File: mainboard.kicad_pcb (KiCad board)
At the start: 2 copper layers, 142 parts, among them IC1 ATXMEGA128A1U-A, J1 USB, K1 X_MIN, K2 X_MAX, K3 Y_MIN, K4 Y_MAX, K5 Z_MIN, K6 Z_MAX, P1 POWER, P10 USART, P11 TH_HB, P12 TH_EX, P13 TH_HO, P14 LCD, P15 STP_Y, P16 STP_E0, P17 STP_X, P18 STP_E1, P19 STP_Z, P2 PDI, P20 EXTR, P21 HIC_0, P22 HEATBED, P23 HIC_1, P24 FAN_0, P25 FAN_1, P26 LOC_0, P27 LOC_1, P28 INTERFACE, P3 GPIO_B, P4 BEEPER, P5 OPEN_COLL_D, P6 12V, P7 5V, P8 3.3V, P9 I2C, Q1 IRL1404, Q2 IRL1404, Q3 IRL1404, Q4 IRL1404, SW1 Y, SW2 E0, SW3 X, SW4 E1, SW5 Z, U1 NE 4558 D SMD, U10 ULN_2003_A, U2 ULN_2003_A, U3 A4988-BO, U4 A4988-BO, U5 A4988-BO, U6 A4988-BO, U7 A4988-BO, U8 MCP14E10, U9 MCP14E10

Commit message: * Removed numerous errors, schematic now passes ERC test. * Arranged footprints on PCB to prepare for routing
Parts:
- moved D7 197.4 mm to (3.50, 206.0), turned to 270 degrees
- moved D6 174.9 mm to (136.0, 212.0), turned to 270 degrees
- moved D5 172.1 mm to (66.0, 232.5), turned to 270 degrees
- moved P10 171.5 mm to (202.5, 62.5)
- moved P7 161.9 mm to (227.5, 37.0)
- moved C11 159.2 mm to (225.0, 102.5), turned to 180 degrees
- moved P6 136.2 mm to (234.0, 37.0)
- moved R8 135.7 mm to (218.0, 65.0)
- moved R21 131.1 mm to (139.0, 212.5)
- moved R23 125.2 mm to (139.0, 159.0)
- moved R9 115.5 mm to (214.2, 65.1)
- moved D9 114.5 mm to (65.0, 174.0), turned to 270 degrees
- moved D8 113.1 mm to (135.5, 159.0), turned to 270 degrees
- moved C16 105.7 mm to (136.0, 95.5)
- moved RV3 94.4 mm to (136.5, 77.5)
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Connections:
- C11 pad 2: Net-(C11-Pad2) -> +3.3V
- C18 pad 2: Net-(C18-Pad2) -> GND
- C19 pad 2: Net-(C19-Pad2) -> GND
- C20 pad 2: Net-(C20-Pad2) -> GND
- C21 pad 2: Net-(C21-Pad2) -> GND
- C22 pad 2: Net-(C22-Pad2) -> GND
- D5 pad 1: Net-(D5-Pad1) -> E0-STEP
- D6 pad 1: Net-(D6-Pad1) -> Y-STEP
- D7 pad 1: Net-(D7-Pad1) -> E1-STEP
- D8 pad 1: Net-(D8-Pad1) -> X-STEP
- D9 pad 1: Net-(D9-Pad1) -> Z-STEP
- IC1 pad 55: Z_DIR -> X-DIR
- IC1 pad 56: Y_DIR -> Y-DIR
- IC1 pad 57: X_DIR -> Z-DIR
- IC1 pad 58: Z_STEP -> E0-STEP
- IC1 pad 59: Y_STEP -> E1-STEP
- IC1 pad 60: X_STEP -> X-STEP
- IC1 pad 61: E1_STEP -> Y-STEP
- IC1 pad 62: E0_STEP -> Z-STEP
- IC1 pad 65: E0_EN -> E0-EN
- IC1 pad 66: E1_EN -> E1-EN
- IC1 pad 67: Z_EN -> X-EN
- IC1 pad 68: Y_EN -> Y-EN
- IC1 pad 69: X_EN -> Z-EN
- IC1 pad 70: E1_DIR -> E0-DIR
- IC1 pad 71: E0_DIR -> E1-DIR
- P15 pad 1: Net-(P15-Pad1) -> /motortreiber-sub/Y1B
- P15 pad 2: Net-(P15-Pad2) -> /motortreiber-sub/Y1A
- P15 pad 3: Net-(P15-Pad3) -> /motortreiber-sub/Y2B
- P15 pad 4: Net-(P15-Pad4) -> /motortreiber-sub/Y2A
- P16 pad 1: Net-(P16-Pad1) -> /motortreiber-sub/E01B
- P16 pad 2: Net-(P16-Pad2) -> /motortreiber-sub/E01A
- P16 pad 3: Net-(P16-Pad3) -> /motortreiber-sub/E02B
- P16 pad 4: Net-(P16-Pad4) -> /motortreiber-sub/E02A
- P17 pad 1: Net-(P17-Pad1) -> /motortreiber-sub/X1B
- P17 pad 2: Net-(P17-Pad2) -> /motortreiber-sub/X1A
- P17 pad 3: Net-(P17-Pad3) -> /motortreiber-sub/X2B
- P17 pad 4: Net-(P17-Pad4) -> /motortreiber-sub/X2A
- P18 pad 1: Net-(P18-Pad1) -> /motortreiber-sub/E11B
- P18 pad 2: Net-(P18-Pad2) -> /motortreiber-sub/E11A
- P18 pad 3: Net-(P18-Pad3) -> /motortreiber-sub/E12B
- P18 pad 4: Net-(P18-Pad4) -> /motortreiber-sub/E12A
- P19 pad 1: Net-(P19-Pad1) -> /motortreiber-sub/Z1B
- P19 pad 2: Net-(P19-Pad2) -> /motortreiber-sub/Z1A
- P19 pad 3: Net-(P19-Pad3) -> /motortreiber-sub/Z2B
- P19 pad 4: Net-(P19-Pad4) -> /motortreiber-sub/Z2A
- P4 pad 1: Net-(P4-Pad1) -> Net-(C13-Pad2)
- U3 pad 11: Net-(P15-Pad2) -> /motortreiber-sub/Y1B
- U3 pad 12: Net-(P15-Pad1) -> /motortreiber-sub/Y1A
- U3 pad 13: Net-(P15-Pad4) -> /motortreiber-sub/Y2B
- U3 pad 14: Net-(P15-Pad3) -> /motortreiber-sub/Y2A
- U3 pad 15: Net-(C18-Pad2) -> GND
- U3 pad 5: Net-(U3-Pad5) -> +3.3V
- U3 pad 6: Net-(U3-Pad5) -> +3.3V
- U4 pad 11: Net-(P16-Pad2) -> /motortreiber-sub/E01B
- U4 pad 12: Net-(P16-Pad1) -> /motortreiber-sub/E01A
- U4 pad 13: Net-(P16-Pad4) -> /motortreiber-sub/E02B
- U4 pad 14: Net-(P16-Pad3) -> /motortreiber-sub/E02A
- U4 pad 15: Net-(C19-Pad2) -> GND
- U4 pad 5: Net-(U4-Pad5) -> +3.3V
- U4 pad 6: Net-(U4-Pad5) -> +3.3V
- U5 pad 11: Net-(P17-Pad2) -> /motortreiber-sub/X1B
- U5 pad 12: Net-(P17-Pad1) -> /motortreiber-sub/X1A
- U5 pad 13: Net-(P17-Pad4) -> /motortreiber-sub/X2B
- U5 pad 14: Net-(P17-Pad3) -> /motortreiber-sub/X2A
- U5 pad 15: Net-(C20-Pad2) -> GND
- U5 pad 5: Net-(U5-Pad5) -> +3.3V
- U5 pad 6: Net-(U5-Pad5) -> +3.3V
- U6 pad 11: Net-(P18-Pad2) -> /motortreiber-sub/E11B
- U6 pad 12: Net-(P18-Pad1) -> /motortreiber-sub/E11A
- U6 pad 13: Net-(P18-Pad4) -> /motortreiber-sub/E12B
- U6 pad 14: Net-(P18-Pad3) -> /motortreiber-sub/E12A
- U6 pad 15: Net-(C21-Pad2) -> GND
- U6 pad 5: Net-(U6-Pad5) -> +3.3V
- U6 pad 6: Net-(U6-Pad5) -> +3.3V
- U7 pad 11: Net-(P19-Pad2) -> /motortreiber-sub/Z1B
- U7 pad 12: Net-(P19-Pad1) -> /motortreiber-sub/Z1A
- U7 pad 13: Net-(P19-Pad4) -> /motortreiber-sub/Z2B
- U7 pad 14: Net-(P19-Pad3) -> /motortreiber-sub/Z2A
- U7 pad 15: Net-(C22-Pad2) -> GND
- U7 pad 5: Net-(U7-Pad5) -> +3.3V
- U7 pad 6: Net-(U7-Pad5) -> +3.3V

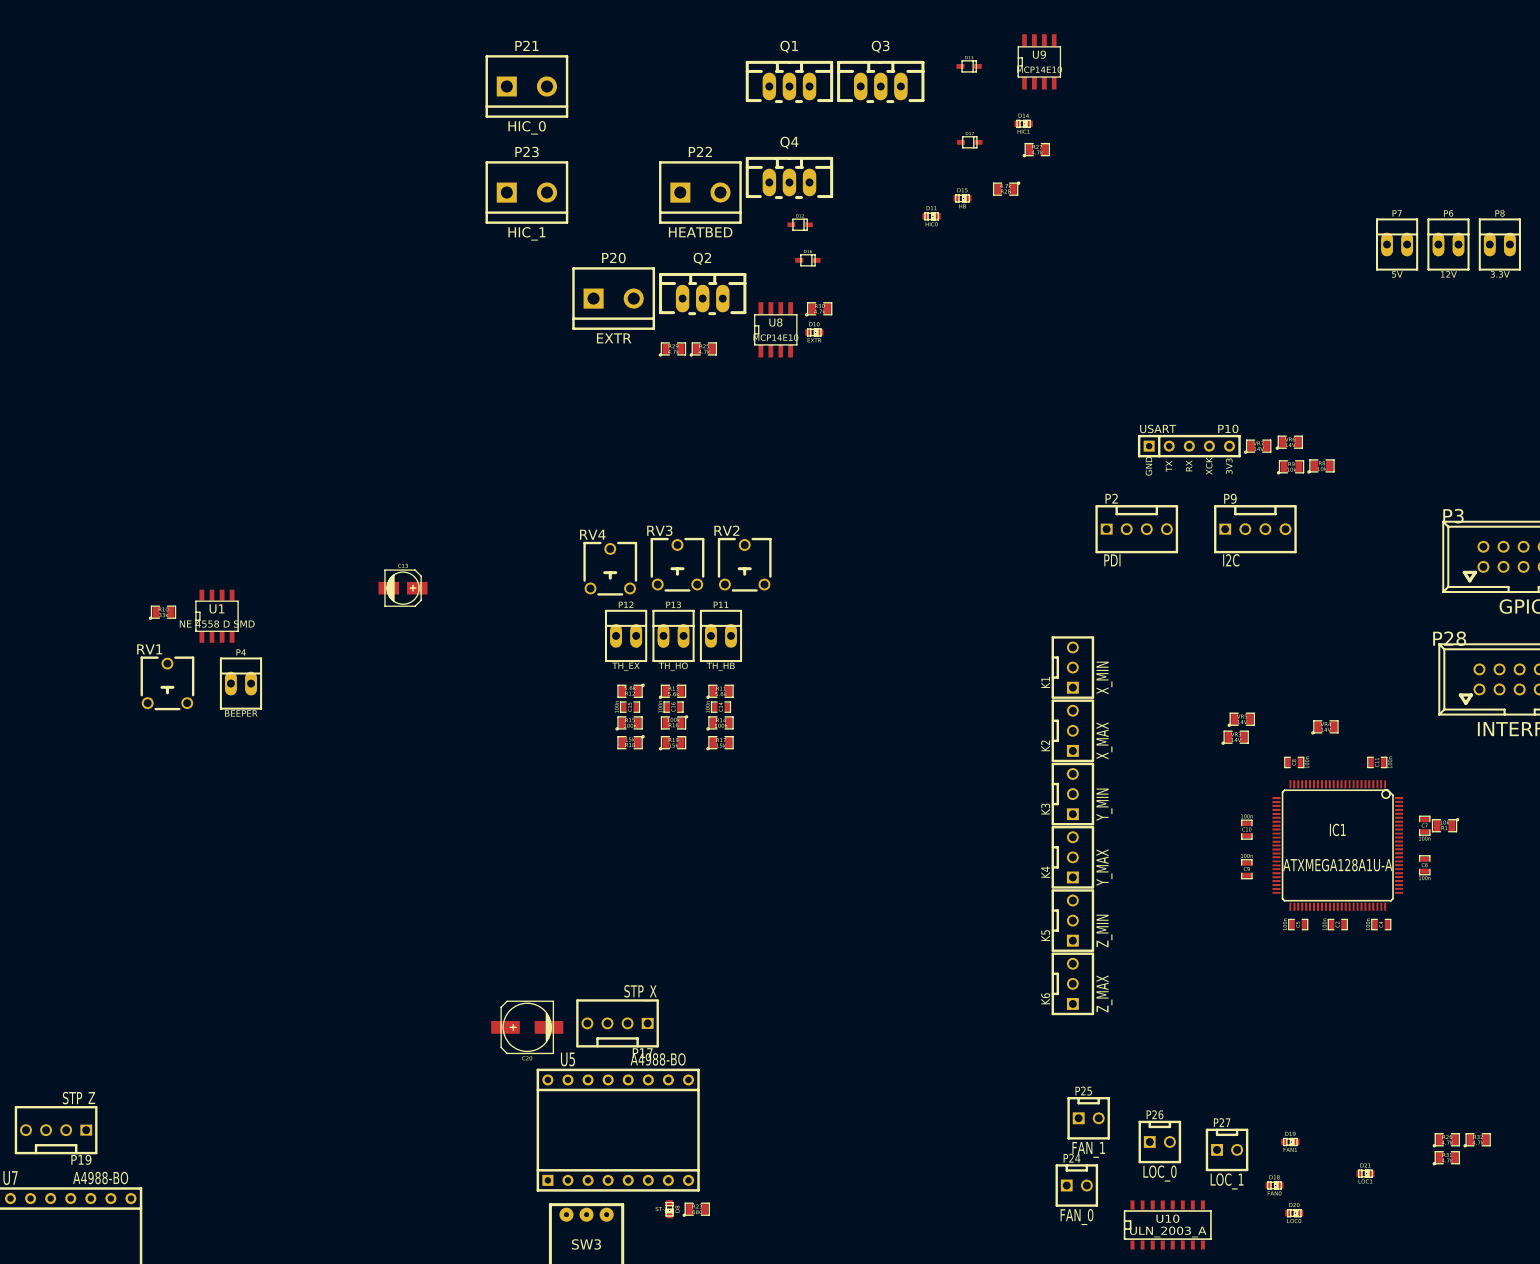
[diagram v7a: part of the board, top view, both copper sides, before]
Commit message: Added decoupling caps for MOSFET drivers
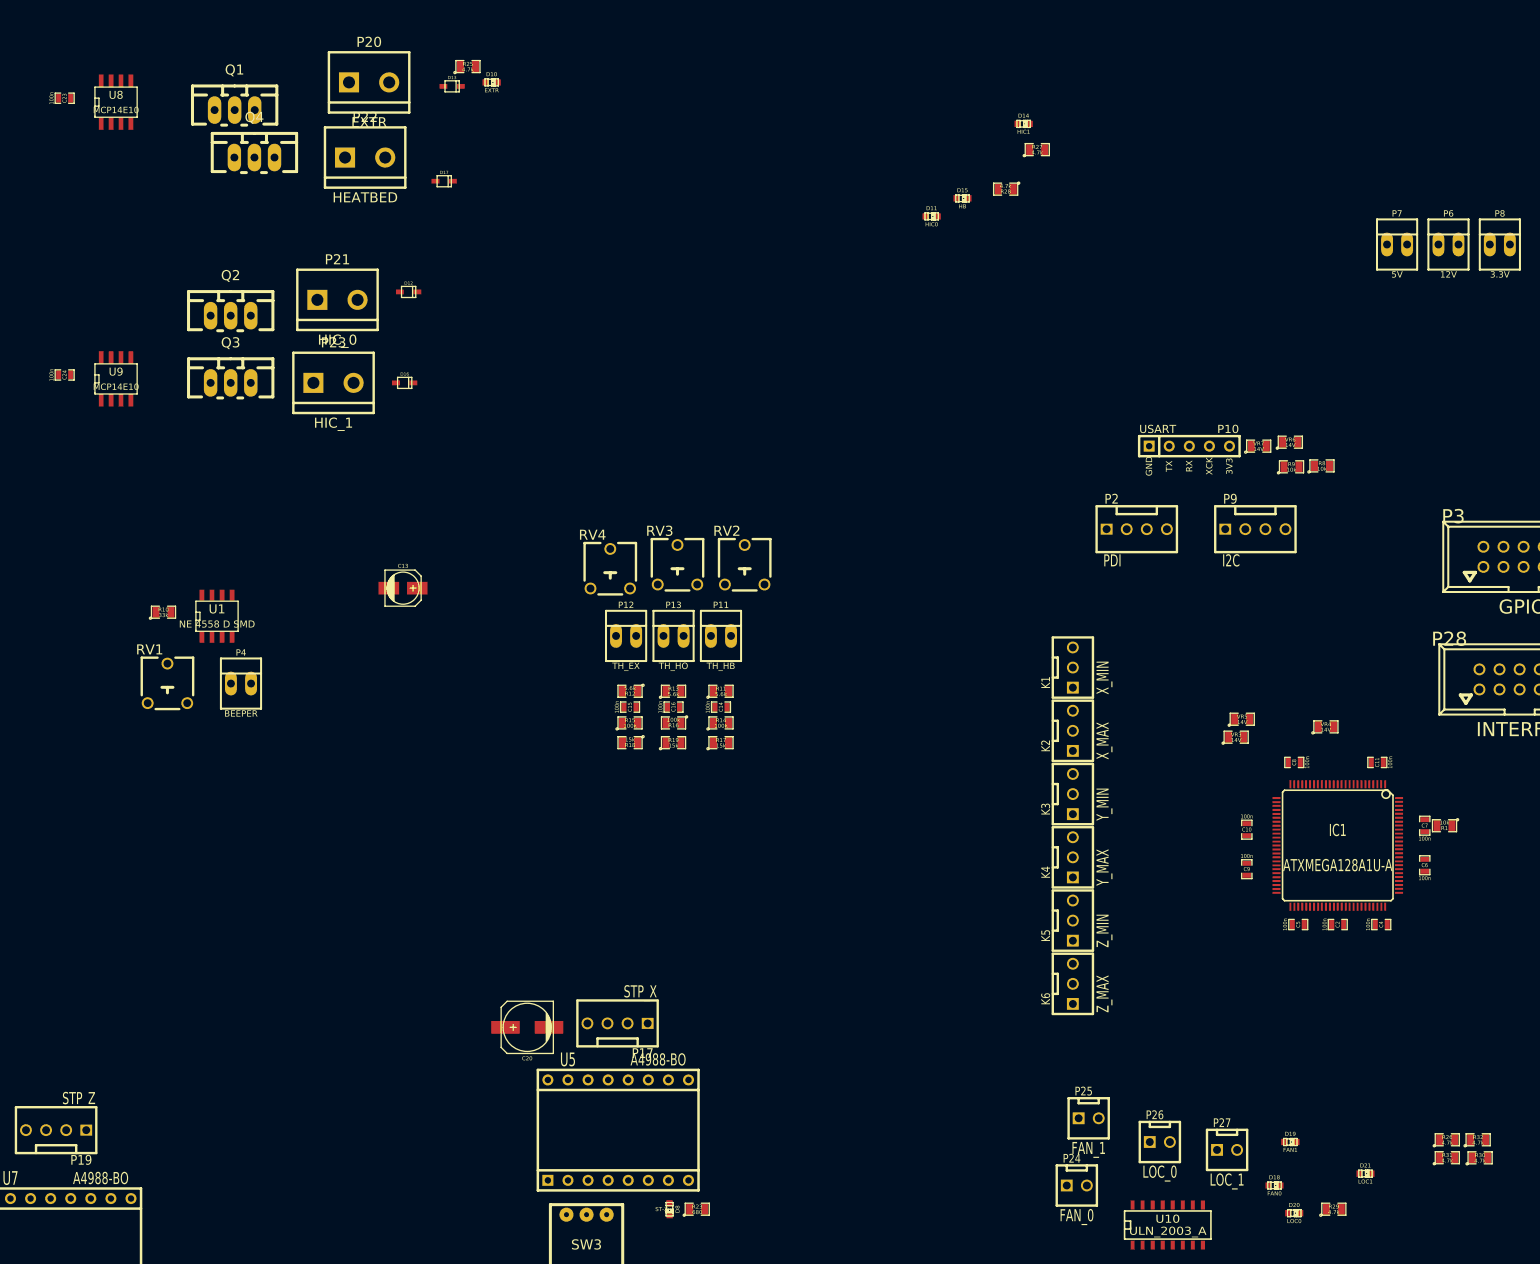
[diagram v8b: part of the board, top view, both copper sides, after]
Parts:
- added C23: 100n, SMD_Packages:SM0603_Capa, F.Cu at (59.0, 18.5)
- added C24: 100n, SMD_Packages:SM0603_Capa, F.Cu at (59.0, 53.5)
- moved R29 137.1 mm to (219.5, 159.0)
- moved R30 136.0 mm to (238.0, 152.5)
- moved U9 123.5 mm to (65.5, 54.0)
- moved Q3 90.4 mm to (80.0, 54.5)
- moved U8 88.3 mm to (65.5, 19.0)
- moved Q1 70.2 mm to (80.5, 20.0)
- moved Q4 67.7 mm to (83.0, 26.0)
- moved D17 66.6 mm to (107.0, 29.0)
- moved D13 65.4 mm to (108.0, 17.0)
- moved Q2 59.7 mm to (80.0, 46.0)
- moved D16 53.3 mm to (102.0, 54.5)
- moved D10 51.6 mm to (113.0, 16.5)
- moved D12 50.2 mm to (102.5, 43.0)
- moved R25 46.6 mm to (110.0, 14.5)
- moved P22 42.6 mm to (97.0, 26.0)
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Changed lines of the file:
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@@
 (kicad_pcb (version 3) (host pcbnew "(2014-04-22 BZR 4817)-product")
   (general
-    (links 408)
-    (no_connects 408)
+    (links 412)
+    (no_connects 410)
     (area 0 0 0 0)
     (thickness 1.6)
@@
     (tracks 0)
     (zones 0)
-    (modules 142)
+    (modules 144)
     (nets 179)
   )
@@
   )
   (module LEDs:LED-0603 (layer F.Cu)
-    (at 153.80208 48.1261)
+    (at 113 16.5)
     (descr "LED 0603 smd package")
     (tags "LED led 0603 SMD smd SMT smt smdled SMDLED smtled SMTLED")
@@
   )
   (module Connect:bornier2 (layer F.Cu)
-    (at 128.426401 43.838)
+    (at 97.5 16.5)
     (descr "Bornier d'alimentation 2 pins")
     (tags DEV)
@@
   )
   (module Connect:bornier2 (layer F.Cu)
-    (at 117.456401 17.018)
+    (at 93.5 44)
     (descr "Bornier d'alimentation 2 pins")
     (tags DEV)
@@
   )
   (module Connect:bornier2 (layer F.Cu)
-    (at 139.396401 30.428)
+    (at 97 26)
     (descr "Bornier d'alimentation 2 pins")
     (tags DEV)
@@
   )
   (module Connect:bornier2 (layer F.Cu)
-    (at 117.456401 30.428)
+    (at 93 54.5)
     (descr "Bornier d'alimentation 2 pins")
     (tags DEV)
@@
   )
   (module Transistors_TO-220:TO-220_FET-GDS_Vertical_LargePads (layer F.Cu)
-    (at 150.658501 17.018)
+    (at 80.5 20)
     (descr "TO-220, FET-GDS, Vertical, Large Pads,")
     (tags "TO-220, FET-GDS, Vertical, Large Pads,")
@@
   )
   (module Transistors_TO-220:TO-220_FET-GDS_Vertical_LargePads (layer F.Cu)
-    (at 139.688501 43.838)
+    (at 80 46)
     (descr "TO-220, FET-GDS, Vertical, Large Pads,")
     (tags "TO-220, FET-GDS, Vertical, Large Pads,")
@@
   )
   (module Transistors_TO-220:TO-220_FET-GDS_Vertical_LargePads (layer F.Cu)
-    (at 162.208501 17.018)
+    (at 80 54.5)
     (descr "TO-220, FET-GDS, Vertical, Large Pads,")
     (tags "TO-220, FET-GDS, Vertical, Large Pads,")
@@
   )
   (module Transistors_TO-220:TO-220_FET-GDS_Vertical_LargePads (layer F.Cu)
-    (at 150.658501 29.158)
+    (at 83 26)
     (descr "TO-220, FET-GDS, Vertical, Large Pads,")
     (tags "TO-220, FET-GDS, Vertical, Large Pads,")
@@
   )
   (module SMD_Packages:SM0805 (layer F.Cu)
-    (at 139.891531 50.205596)
+    (at 110 14.5)
     (attr smd)
     (fp_text reference R25 (at 0 -0.3175) (layer F.SilkS)
@@
   )
   (module SMD_Packages:SM0805 (layer F.Cu)
-    (at 135.991531 50.205596)
+    (at 219.5 159)
     (attr smd)
     (fp_text reference R29 (at 0 -0.3175) (layer F.SilkS)
@@
   )
   (module SMD_Packages:SM0805 (layer F.Cu)
-    (at 154.481531 45.125596)
+    (at 238 152.5)
     (attr smd)
     (fp_text reference R30 (at 0 -0.3175) (layer F.SilkS)
@@
   )
   (module SOIC_Packages:SOIC-8_N (layer F.Cu)
-    (at 148.931858 47.794)
+    (at 65.5 19)
     (descr "module CMS SOJ 8 pins etroit")
     (tags "CMS SOJ")
@@
   )
   (module SOIC_Packages:SOIC-8_N (layer F.Cu)
-    (at 182.261858 13.914)
+    (at 65.5 54)
     (descr "module CMS SOJ 8 pins etroit")
     (tags "CMS SOJ")
@@
   )
   (module smd-diode:SOD323 (layer F.Cu)
-    (at 152 34.5)
+    (at 102.5 43)
     (descr SOD323)
     (fp_text reference D12 (at 0 -1.09982) (layer F.SilkS)
@@
   )
   (module smd-diode:SOD323 (layer F.Cu)
-    (at 173.38512 14.478)
+    (at 108 17)
     (descr SOD323)
     (fp_text reference D13 (at 0 -1.09982) (layer F.SilkS)
@@
   )
   (module smd-diode:SOD323 (layer F.Cu)
-    (at 153 39)
+    (at 102 54.5)
     (descr SOD323)
     (fp_text reference D16 (at 0 -1.09982) (layer F.SilkS)
@@
   )
   (module smd-diode:SOD323 (layer F.Cu)
-    (at 173.46512 24.078)
+    (at 107 29)
     (descr SOD323)
     (fp_text reference D17 (at 0 -1.09982) (layer F.SilkS)
@@
       (net 178 /motortreiber-sub/Z2A))
   )
+  (module SMD_Packages:SM0603_Capa (layer F.Cu)
+    (at 59 18.5)
+    (attr smd)
+    (fp_text reference C23 (at 0 0 90) (layer F.SilkS)
+      (effects (font (size 0.508 0.4572) (thickness 0.1143)))
+    )
+    (fp_text value 100n (at -1.651 0 90) (layer F.SilkS)
+      (effects (font (size 0.508 0.4572) (thickness 0.1143)))
+    )
+    (fp_line (start 0.50038 0.65024) (end 1.19888 0.65024) (layer F.SilkS) (width 0.11938))
+    (fp_line (start -0.50038 0.65024) (end -1.19888 0.65024) (layer F.SilkS) (width 0.11938))
+    (fp_line (start 0.50038 -0.65024) (end 1.19888 -0.65024) (layer F.SilkS) (width 0.11938))
+    (fp_line (start -1.19888 -0.65024) (end -0.50038 -0.65024) (layer F.SilkS) (width 0.11938))
+    (fp_line (start 1.19888 -0.635) (end 1.19888 0.635) (layer F.SilkS) (width 0.11938))
+    (fp_line (start -1.19888 0.635) (end -1.19888 -0.635) (layer F.SilkS) (width 0.11938))
+    (pad 1 smd rect (at -0.762 0) (size 0.635 1.143) (layers F.Cu F.Paste F.Mask)
+      (net 1 +12V))
+    (pad 2 smd rect (at 0.762 0) (size 0.635 1.143) (layers F.Cu F.Paste F.Mask)
+      (net 2 GND))
+    (model smd\capacitors\C0603.wrl
+      (at (xyz 0 0 0.001))
+      (scale (xyz 0.5 0.5 0.5))
+      (rotate (xyz 0 0 0))
+    )
+  )
+  (module SMD_Packages:SM0603_Capa (layer F.Cu)
+    (at 59 53.5)
+    (attr smd)
+    (fp_text reference C24 (at 0 0 90) (layer F.SilkS)
+      (effects (font (size 0.508 0.4572) (thickness 0.1143)))
+    )
+    (fp_text value 100n (at -1.651 0 90) (layer F.SilkS)
+      (effects (font (size 0.508 0.4572) (thickness 0.1143)))
+    )
+    (fp_line (start 0.50038 0.65024) (end 1.19888 0.65024) (layer F.SilkS) (width 0.11938))
+    (fp_line (start -0.50038 0.65024) (end -1.19888 0.65024) (layer F.SilkS) (width 0.11938))
+    (fp_line (start 0.50038 -0.65024) (end 1.19888 -0.65024) (layer F.SilkS) (width 0.11938))
+    (fp_line (start -1.19888 -0.65024) (end -0.50038 -0.65024) (layer F.SilkS) (width 0.11938))
+    (fp_line (start 1.19888 -0.635) (end 1.19888 0.635) (layer F.SilkS) (width 0.11938))
+    (fp_line (start -1.19888 0.635) (end -1.19888 -0.635) (layer F.SilkS) (width 0.11938))
+    (pad 1 smd rect (at -0.762 0) (size 0.635 1.143) (layers F.Cu F.Paste F.Mask)
+      (net 1 +12V))
+    (pad 2 smd rect (at 0.762 0) (size 0.635 1.143) (layers F.Cu F.Paste F.Mask)
+      (net 2 GND))
+    (model smd\capacitors\C0603.wrl
+      (at (xyz 0 0 0.001))
+      (scale (xyz 0.5 0.5 0.5))
+      (rotate (xyz 0 0 0))
+    )
+  )
 )
